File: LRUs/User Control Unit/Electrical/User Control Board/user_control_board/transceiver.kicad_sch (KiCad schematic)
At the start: 1 part, among them U2 RFM69HW

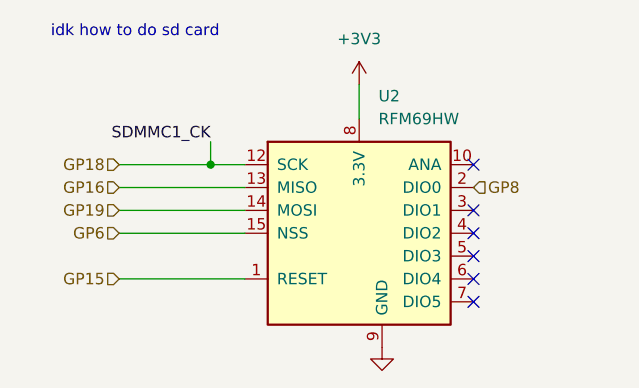
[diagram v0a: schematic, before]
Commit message: transceiver finished based on spi
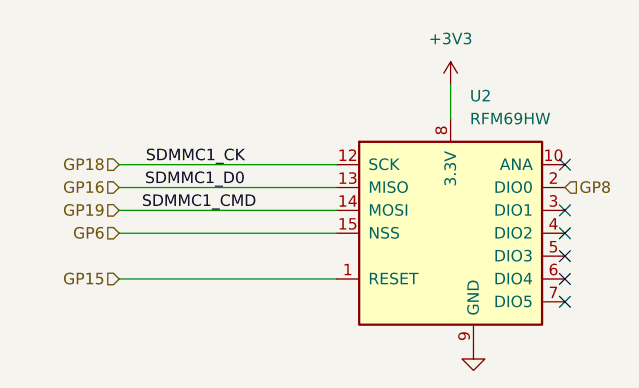
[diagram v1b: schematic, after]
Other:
- note removed: "idk how to do sd card"
- moved on the sheet: U2
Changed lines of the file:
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@@
 	(generator_version "10.0")
 	(paper "A4")
-	(text "idk how to do sd card"
-		(exclude_from_sim no)
-		(at 84.328 79.248 0)
-		(effects
-			(font
-				(size 1.27 1.27)
-			)
-		)
-	)
-	(junction
-		(at 92.71 93.98)
-		(diameter 0)
-		(color 0 0 0 0)
-	)
-	(no_connect
-		(at 121.92 104.14)
-	)
-	(no_connect
-		(at 121.92 99.06)
-	)
-	(no_connect
-		(at 121.92 101.6)
-	)
-	(no_connect
-		(at 121.92 93.98)
-	)
-	(no_connect
-		(at 121.92 109.22)
-	)
-	(no_connect
-		(at 121.92 106.68)
-	)
-	(wire
-		(pts
-			(xy 92.71 93.98) (xy 96.52 93.98)
-		)
-		(stroke
-			(width 0)
-			(type default)
-		)
-	)
-	(wire
-		(pts
-			(xy 82.55 96.52) (xy 96.52 96.52)
-		)
-		(stroke
-			(width 0)
-			(type default)
-		)
-	)
-	(wire
-		(pts
-			(xy 82.55 101.6) (xy 96.52 101.6)
-		)
-		(stroke
-			(width 0)
-			(type default)
-		)
-	)
-	(wire
-		(pts
-			(xy 82.55 106.68) (xy 96.52 106.68)
-		)
-		(stroke
-			(width 0)
-			(type default)
-		)
-	)
-	(wire
-		(pts
-			(xy 92.71 91.44) (xy 92.71 93.98)
-		)
-		(stroke
-			(width 0)
-			(type default)
-		)
-	)
-	(wire
-		(pts
-			(xy 82.55 99.06) (xy 96.52 99.06)
-		)
-		(stroke
-			(width 0)
-			(type default)
-		)
-	)
-	(wire
-		(pts
-			(xy 82.55 93.98) (xy 92.71 93.98)
-		)
-		(stroke
-			(width 0)
-			(type default)
-		)
-	)
-	(wire
-		(pts
-			(xy 109.22 85.09) (xy 109.22 88.9)
+	(no_connect
+		(at 132.08 104.14)
+	)
+	(no_connect
+		(at 132.08 99.06)
+	)
+	(no_connect
+		(at 132.08 101.6)
+	)
+	(no_connect
+		(at 132.08 93.98)
+	)
+	(no_connect
+		(at 132.08 109.22)
+	)
+	(no_connect
+		(at 132.08 106.68)
+	)
+	(wire
+		(pts
+			(xy 82.55 96.52) (xy 106.68 96.52)
+		)
+		(stroke
+			(width 0)
+			(type default)
+		)
+	)
+	(wire
+		(pts
+			(xy 82.55 101.6) (xy 106.68 101.6)
+		)
+		(stroke
+			(width 0)
+			(type default)
+		)
+	)
+	(wire
+		(pts
+			(xy 82.55 106.68) (xy 106.68 106.68)
+		)
+		(stroke
+			(width 0)
+			(type default)
+		)
+	)
+	(wire
+		(pts
+			(xy 82.55 99.06) (xy 106.68 99.06)
+		)
+		(stroke
+			(width 0)
+			(type default)
+		)
+	)
+	(wire
+		(pts
+			(xy 82.55 93.98) (xy 106.68 93.98)
+		)
+		(stroke
+			(width 0)
+			(type default)
+		)
+	)
+	(wire
+		(pts
+			(xy 119.38 85.09) (xy 119.38 88.9)
 		)
 		(stroke
@@
 	)
 	(label "SDMMC1_CK"
-		(at 92.71 91.44 180)
+		(at 96.52 93.98 180)
 		(effects
 			(font
@@
 		)
 	)
+	(label "SDMMC1_D0"
+		(at 96.52 96.52 180)
+		(effects
+			(font
+				(size 1.27 1.27)
+			)
+			(justify right bottom)
+		)
+	)
+	(label "SDMMC1_CMD"
+		(at 97.79 99.06 180)
+		(effects
+			(font
+				(size 1.27 1.27)
+			)
+			(justify right bottom)
+		)
+	)
 	(hierarchical_label "GP19"
 		(shape input)
@@
 	(hierarchical_label "GP8"
 		(shape input)
-		(at 121.92 96.52 0)
+		(at 132.08 96.52 0)
 		(effects
 			(font
@@
 	(symbol
 		(lib_id "power:+5V")
-		(at 109.22 85.09 0)
+		(at 119.38 85.09 0)
 		(unit 1)
 		(body_style 1)
@@
 		(fields_autoplaced yes)
 		(property "Reference" "#PWR019"
-			(at 109.22 88.9 0)
+			(at 119.38 88.9 0)
 			(hide yes)
 			(show_name no)
@@
 		)
 		(property "Value" "+3V3"
-			(at 109.22 80.01 0)
+			(at 119.38 80.01 0)
 			(show_name no)
 			(do_not_autoplace no)
@@
 		)
 		(property "Footprint" ""
-			(at 109.22 85.09 0)
+			(at 119.38 85.09 0)
 			(hide yes)
 			(show_name no)
@@
 		)
 		(property "Datasheet" ""
-			(at 109.22 85.09 0)
+			(at 119.38 85.09 0)
 			(hide yes)
 			(show_name no)
@@
 		)
 		(property "Description" "Power symbol creates a global label with name \"+5V\""
-			(at 109.22 85.09 0)
+			(at 119.38 85.09 0)
 			(hide yes)
 			(show_name no)
@@
 	(symbol
 		(lib_id "RF_Module:RFM69HW")
-		(at 109.22 101.6 0)
+		(at 119.38 101.6 0)
 		(unit 1)
 		(body_style 1)
@@
 		(fields_autoplaced yes)
 		(property "Reference" "U2"
-			(at 111.3633 86.36 0)
+			(at 121.5233 86.36 0)
 			(show_name no)
 			(do_not_autoplace no)
@@
 		)
 		(property "Value" "RFM69HW"
-			(at 111.3633 88.9 0)
+			(at 121.5233 88.9 0)
 			(show_name no)
 			(do_not_autoplace no)
@@
 		)
 		(property "Footprint" "RF_Module:HOPERF_RFM69HW"
-			(at 109.22 116.84 0)
+			(at 119.38 116.84 0)
 			(hide yes)
 			(show_name no)
@@
 		)
 		(property "Datasheet" "https://www.hoperf.com/data/upload/portal/20181127/5bfcbb56f1fd7.pdf"
-			(at 109.22 109.22 0)
+			(at 119.38 109.22 0)
 			(hide yes)
 			(show_name no)
@@
 		)
 		(property "Description" "ISM Radio Transceiver Module, SPI interface"
-			(at 109.22 101.6 0)
+			(at 119.38 101.6 0)
 			(hide yes)
 			(show_name no)
@@
 	(symbol
 		(lib_id "power:GND")
-		(at 111.76 114.3 0)
+		(at 121.92 114.3 0)
 		(unit 1)
 		(body_style 1)
@@
 		(fields_autoplaced yes)
 		(property "Reference" "#PWR020"
-			(at 111.76 120.65 0)
+			(at 121.92 120.65 0)
 			(hide yes)
 			(show_name no)
@@
 		)
 		(property "Value" "GND"
-			(at 111.76 119.38 0)
+			(at 121.92 119.38 0)
 			(hide yes)
 			(show_name no)
@@
 		)
 		(property "Footprint" ""
-			(at 111.76 114.3 0)
+			(at 121.92 114.3 0)
 			(hide yes)
 			(show_name no)
@@
 		)
 		(property "Datasheet" ""
-			(at 111.76 114.3 0)
+			(at 121.92 114.3 0)
 			(hide yes)
 			(show_name no)
@@
 		)
 		(property "Description" "Power symbol creates a global label with name \"GND\" , ground"
-			(at 111.76 114.3 0)
-			(hide yes)
-			(show_name no)
+			(at 121.92 114.3 0)
+			(hide yes)
+			(show_name no)
